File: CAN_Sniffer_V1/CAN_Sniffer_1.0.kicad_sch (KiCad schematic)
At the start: 6 parts, among them J3 Conn_01x04_Pin, J4 USB_B_Micro, U4 TPS7B8750QDDARQ1

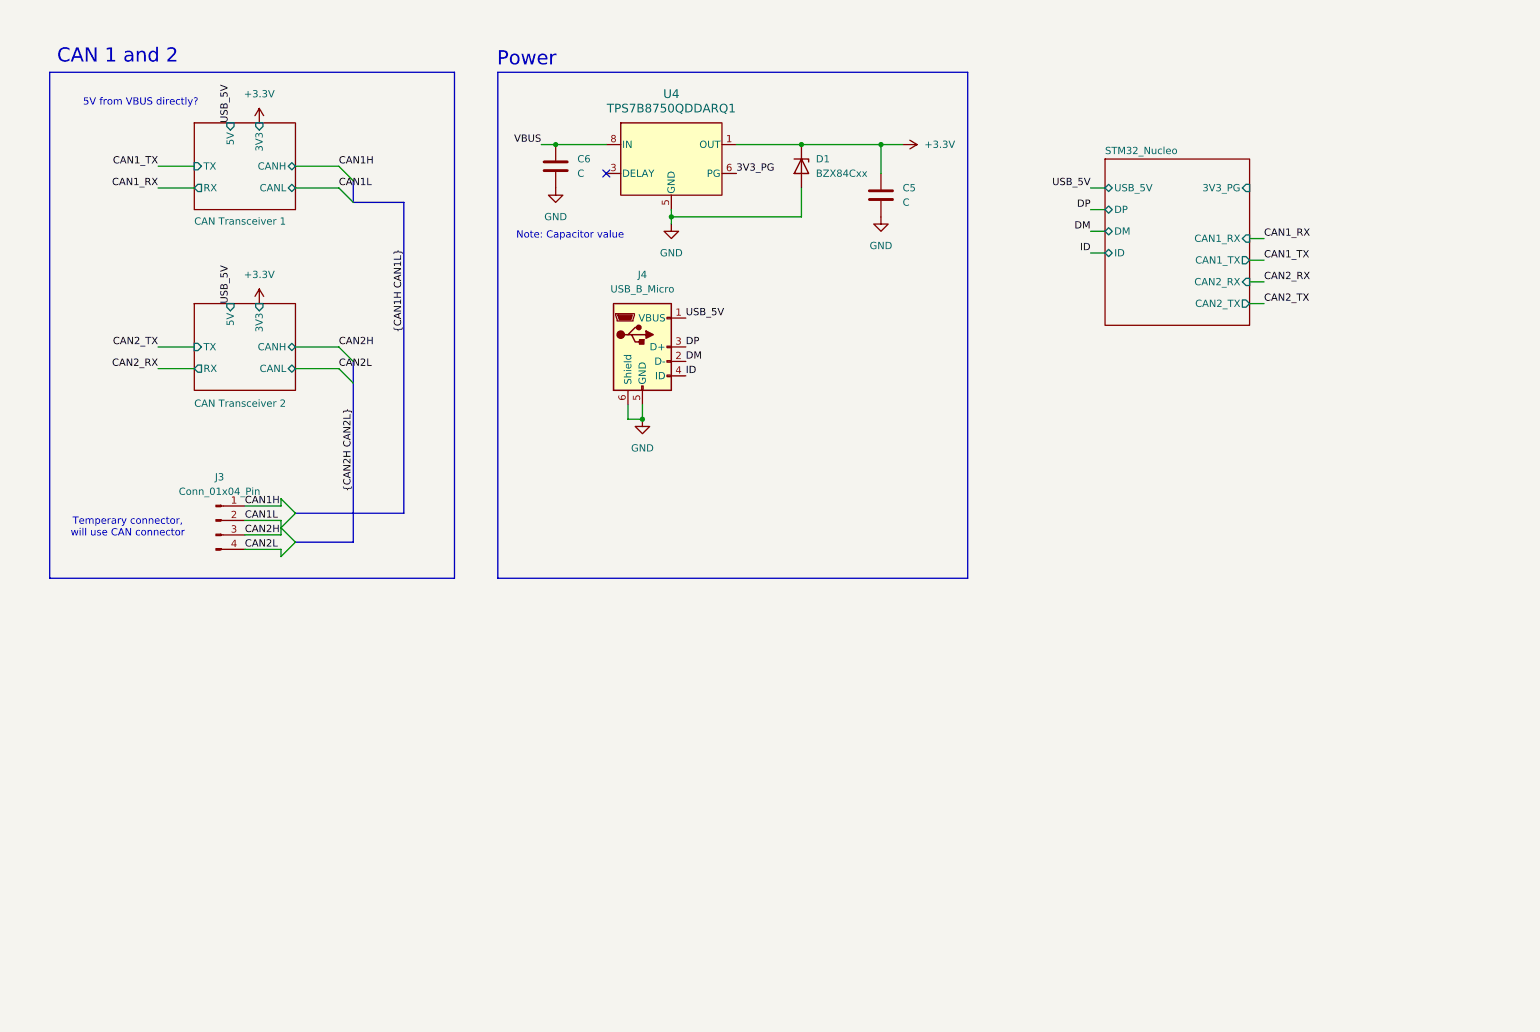
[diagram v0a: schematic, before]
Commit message: changed power schematics and STM32, added MicroSD card connector and LCD display
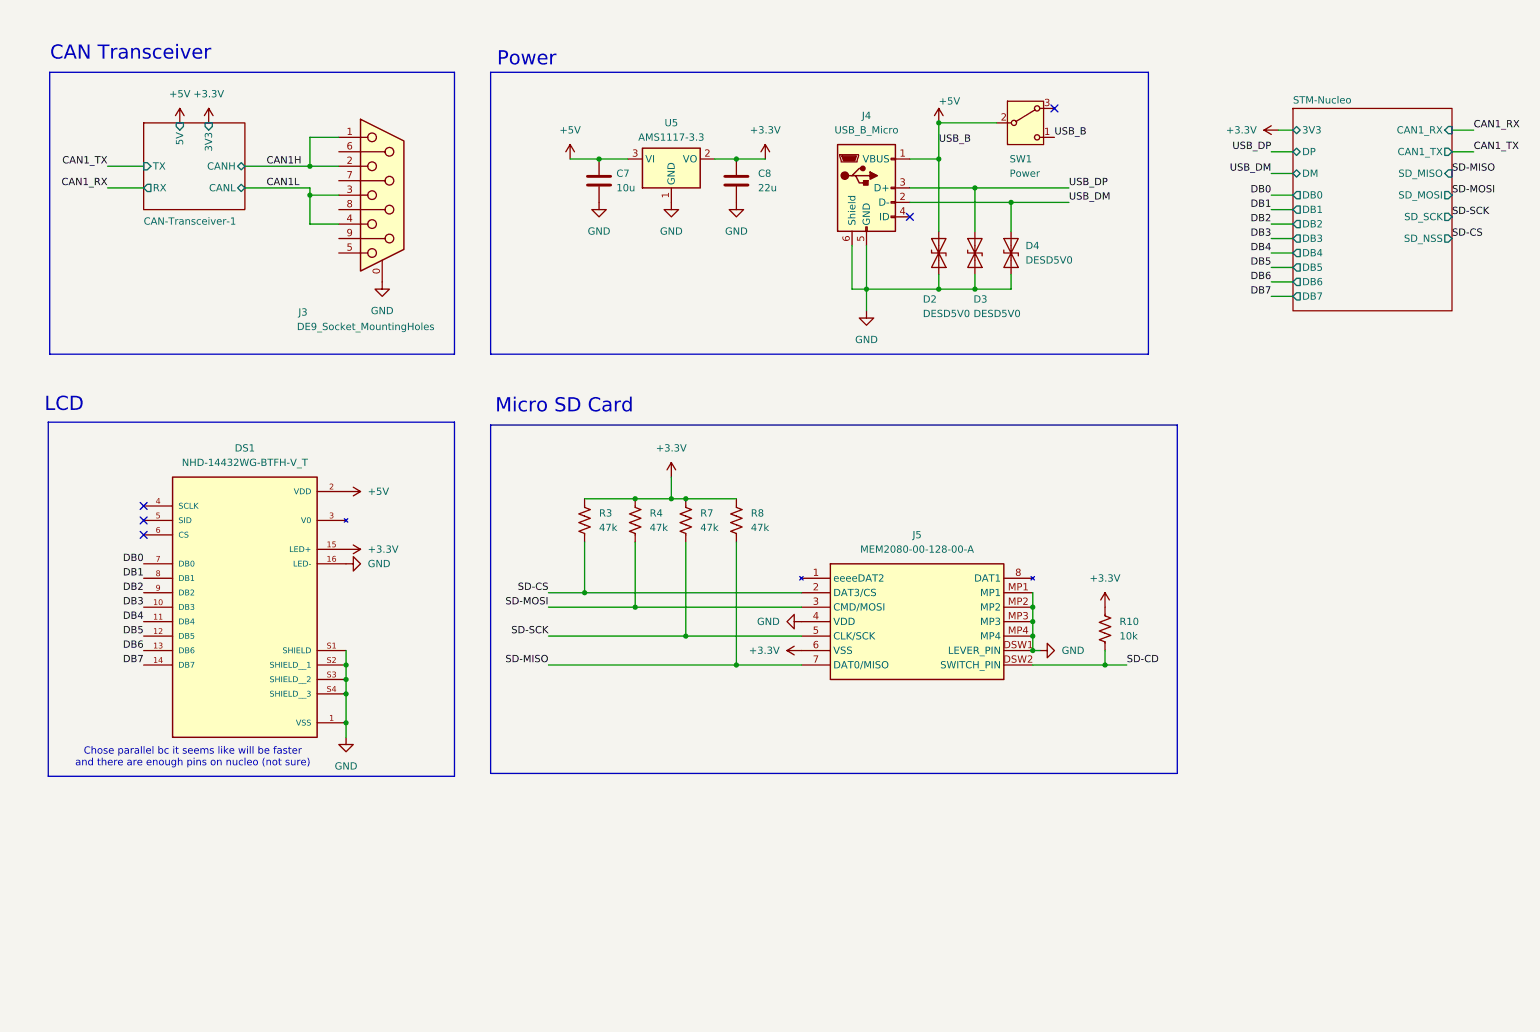
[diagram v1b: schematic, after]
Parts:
- removed C5, C6: C, symbol Device:C
- removed D1: BZX84Cxx, Package_TO_SOT_SMD:SOT-23, symbol Diode:BZX84Cxx
- removed J3: Conn_01x04_Pin, Connector_PinSocket_2.54mm:PinSocket_1x04_P2.54mm_Vertical, symbol Connector:Conn_01x04_Pin
- removed U4: TPS7B8750QDDARQ1, DDA0008J-IPC_A, symbol _LDO:TPS7B8750QDDARQ1
- added C7: 10u, Capacitor_SMD:C_0805_2012Metric_Pad1.18x1.45mm_HandSolder, symbol Device:C
- added C8: 22u, Capacitor_SMD:C_0805_2012Metric_Pad1.18x1.45mm_HandSolder, symbol Device:C
- added D2, D3, D4: DESD5V0, DESD5V0U1BA-7:IC6_AP22653AW6-7_DIO, symbol Diode:ESD131-B1-W0201
- added DS1: NHD-14432WG-BTFH-V_T, NHD-14432WG-BTFH-V_T:LCD_NHD-14432WG-BTFH-V_T, symbol NHD-14432WG-BTFH-V_T:NHD-14432WG-BTFH-V_T
- added J3: DE9_Socket_MountingHoles, Connector_Dsub:DSUB-9_Socket_Horizontal_P2.77x2.84mm_EdgePinOffset7.70mm_Housed_MountingHolesOffset9.12mm, symbol Connector:DE9_Socket_MountingHoles
- added J5: MEM2080-00-128-00-A, Mouser_Parts:MEM20800012800A, symbol Mouser_Parts:MEM2080-00-128-00-A
- added R10: 10k, Resistor_SMD:R_0805_2012Metric_Pad1.20x1.40mm_HandSolder, symbol Device:R_US
- added R3, R4, R7, R8: 47k, Resistor_SMD:R_0805_2012Metric_Pad1.20x1.40mm_HandSolder, symbol Device:R_US
- added SW1: Power, Button_Switch_SMD:Nidec_Copal_CAS-120A, symbol Switch:SW_Nidec_CAS-120A1
- added U5: AMS1117-3.3, Package_TO_SOT_SMD:SOT-223-3_TabPin2, symbol Regulator_Linear:AMS1117-3.3
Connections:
- net +3.3V: now also C8.1, DS1.15 (LED+), J5.6 (VSS), R10.2, R3.1, R4.1, R7.1, R8.1, U5.2 (VO)
- net CAN1H: now also J3.1, J3.2
- net CAN1L: now also J3.3, J3.4
- net GND: now also C7.2, C8.2, D2.1 (A1), D3.1 (A1), D4.1 (A1), DS1.1 (VSS), DS1.16 (LED-), DS1.S1 (SHIELD), DS1.S2 (SHIELD__1), DS1.S3 (SHIELD__2), DS1.S4 (SHIELD__3), J3.0 (PAD), J5.4 (VDD), J5.DSW1 (LEVER_PIN), J5.MP1, J5.MP2, J5.MP3, J5.MP4, U5.1 (GND)
- net DM renamed USB_DM
- net USB_DM: now also D4.2 (A2)
- net DP renamed USB_DP
- net USB_DP: now also D3.2 (A2)
- net ID: no longer names the net of J4.4 (ID)
- net USB_5V renamed +5V
- net +5V: now also C7.1, D2.2 (A2), DS1.2 (VDD), SW1.1 (C), SW1.2 (B), U5.3 (VI)
- new net DB0: DS1.7 (DB0)
- new net DB1: DS1.8 (DB1)
- new net DB2: DS1.9 (DB2)
- new net DB3: DS1.10 (DB3)
- new net DB4: DS1.11 (DB4)
- new net DB5: DS1.12 (DB5)
- new net DB6: DS1.13 (DB6)
- new net DB7: DS1.14 (DB7)
- new net SD-CD: J5.DSW2 (SWITCH_PIN), R10.1
- new net SD-CS: J5.2 (DAT3/CS), R3.2
- new net SD-MISO: J5.7 (DAT0/MISO), R8.2
- new net SD-MOSI: J5.3 (CMD/MOSI), R4.2
- new net SD-SCK: J5.5 (CLK/SCK), R7.2
- no-connect marks 1 -> 5
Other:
- sheet CAN Transceiver 1 renamed CAN-Transceiver-1
- removed sheet CAN Transceiver 2
- removed sheet STM32_Nucleo
- added sheet STM-Nucleo (STM32-Nucleo.kicad_sch)
- note added: "CAN Transceiver"
- note added: "Chose parallel bc it seems like will be faster and there are enough pins on nucleo (not sure)"
- note added: "LCD"
- note added: "Micro SD Card"
- note removed: "5V from VBUS directly?"
- note removed: "CAN 1 and 2"
- note removed: "Note: Capacitor value"
- note removed: "Temperary connector, will use CAN connector"
- moved on the sheet: J4

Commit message: changed power schem, pinouts, first iteration layout
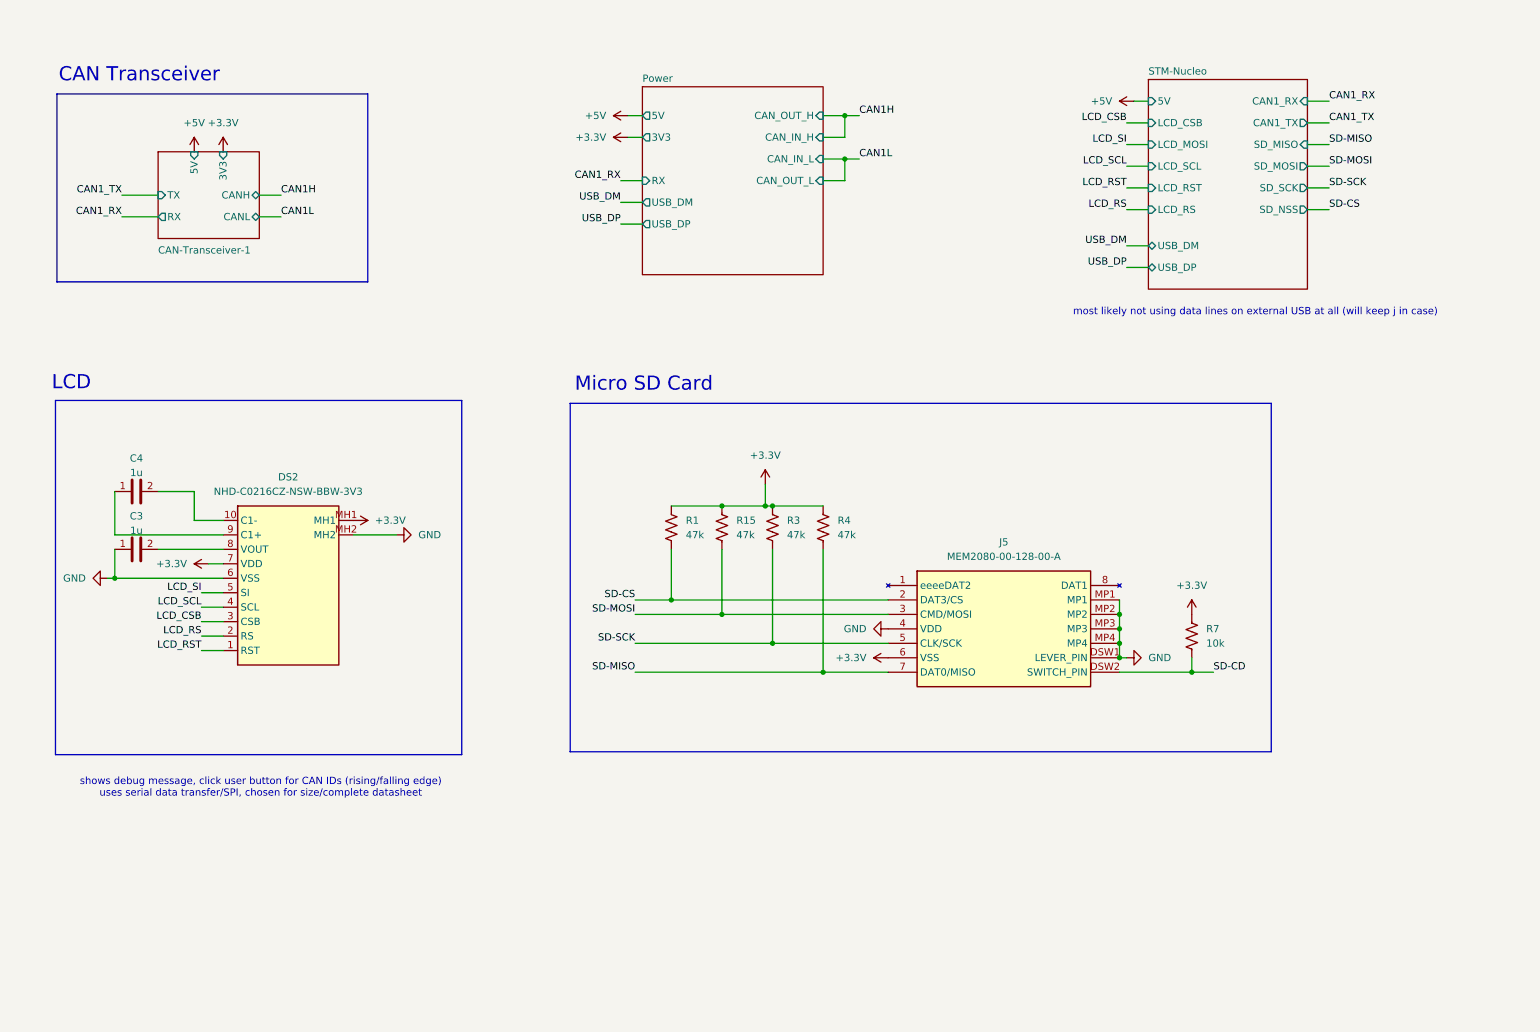
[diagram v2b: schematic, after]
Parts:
- removed C7: 10u, Capacitor_SMD:C_0805_2012Metric_Pad1.18x1.45mm_HandSolder, symbol Device:C
- removed C8: 22u, Capacitor_SMD:C_0805_2012Metric_Pad1.18x1.45mm_HandSolder, symbol Device:C
- removed D2, D3, D4: DESD5V0, DESD5V0U1BA-7:IC6_AP22653AW6-7_DIO, symbol Diode:ESD131-B1-W0201
- removed DS1: NHD-14432WG-BTFH-V_T, NHD-14432WG-BTFH-V_T:LCD_NHD-14432WG-BTFH-V_T, symbol NHD-14432WG-BTFH-V_T:NHD-14432WG-BTFH-V_T
- removed J3: DE9_Socket_MountingHoles, Connector_Dsub:DSUB-9_Socket_Horizontal_P2.77x2.84mm_EdgePinOffset7.70mm_Housed_MountingHolesOffset9.12mm, symbol Connector:DE9_Socket_MountingHoles
- removed J4: USB_B_Micro, Connector_USB:USB_Micro-AB_Molex_47590-0001, symbol Connector:USB_B_Micro
- removed R10: 10k, Resistor_SMD:R_0805_2012Metric_Pad1.20x1.40mm_HandSolder, symbol Device:R_US
- removed R3, R4, R7, R8: 47k, Resistor_SMD:R_0805_2012Metric_Pad1.20x1.40mm_HandSolder, symbol Device:R_US
- removed SW1: Power, Button_Switch_SMD:Nidec_Copal_CAS-120A, symbol Switch:SW_Nidec_CAS-120A1
- removed U5: AMS1117-3.3, Package_TO_SOT_SMD:SOT-223-3_TabPin2, symbol Regulator_Linear:AMS1117-3.3
- added C3, C4: 1u, Capacitor_SMD:C_0603_1608Metric_Pad1.08x0.95mm_HandSolder, symbol bfr_capacitors:MAJCT168BB7105KTEA01
- added DS2: NHD-C0216CZ-NSW-BBW-3V3, NHD-C0216CZ-NSW-BBW-3V3:NHDC0216CZNSWBBW3V3, symbol NHD-C0216CZ-NSW-BBW-3V3:NHD-C0216CZ-NSW-BBW-3V3
- added R1, R15, R3, R4: 47k, Resistor_SMD:R_0603_1608Metric_Pad0.98x0.95mm_HandSolder, symbol bfr_resistors:RMCF0603FT47K0
- added R7: 10k, Resistor_SMD:R_0603_1608Metric_Pad0.98x0.95mm_HandSolder, symbol bfr_resistors:RMCF0603FT10K0
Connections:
- net +3.3V: now also DS2.7 (VDD), DS2.MH1, R1.2, R15.2, R3.2, R4.2, R7.2
- net GND: now also C3.1, DS2.6 (VSS), DS2.MH2
- net SD-CD: now also R7.1
- net SD-CS: now also R1.1
- net SD-MISO: now also R4.1
- net SD-MOSI: now also R15.1
- net SD-SCK: now also R3.1
- new net: C4.2, DS2.10 (C1-)
- new net: C3.2, DS2.8 (VOUT)
- new net: C4.1, DS2.9 (C1+)
- new net LCD_CSB: DS2.3 (CSB)
- new net LCD_RS: DS2.2 (RS)
- new net LCD_RST: DS2.1 (RST)
- new net LCD_SCL: DS2.4 (SCL)
- new net LCD_SI: DS2.5 (SI)
- no-connect marks 5 -> 0
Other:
- added sheet Power (Power.kicad_sch)
- sheet STM-Nucleo ports: added 5V, LCD_CSB, LCD_MOSI, LCD_RS, LCD_RST, LCD_SCL, USB_DM, USB_DP; removed 3V3, DB0, DB1, DB2, DB3, DB4, DB5, DB6, DB7, DM, DP
- note added: "most likely not using data lines on external USB at all (will keep j in case)"
- note added: "shows debug message, click user button for CAN IDs (rising/falling edge) uses serial data transfer/SPI, chosen for size/complete datasheet"
- note removed: "Chose parallel bc it seems like will be faster and there are enough pins on nucleo (not sure)"
- note removed: "Power"
- moved on the sheet: J5

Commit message: iteration 2 routing
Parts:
- removed R7: 10k, Resistor_SMD:R_0603_1608Metric_Pad0.98x0.95mm_HandSolder, symbol bfr_resistors:RMCF0603FT10K0
- added C14: 10u, Capacitor_SMD:C_0603_1608Metric_Pad1.08x0.95mm_HandSolder, symbol bfr_capacitors:CL10A106MA8NRNC
- added C7, C8, C9: 100n, Capacitor_SMD:C_0603_1608Metric_Pad1.08x0.95mm_HandSolder, symbol bfr_capacitors:06035C104KAT2A
- added R12: 10k, Resistor_SMD:R_0603_1608Metric_Pad0.98x0.95mm_HandSolder, symbol bfr_resistors:RMCF0603FT10K0
- added TP12: LCD-SI, TestPoint:TestPoint_Pad_D1.0mm, symbol Connector:TestPoint
- added TP13, TP14: LCD-SCL, TestPoint:TestPoint_Pad_D1.0mm, symbol Connector:TestPoint
- added TP15: LCD-RST, TestPoint:TestPoint_Pad_D1.0mm, symbol Connector:TestPoint
- added TP16, TP22: LCD_3V3, TestPoint:TestPoint_Pad_D1.0mm, symbol Connector:TestPoint
- added TP17: LCD_VOUT, TestPoint:TestPoint_Pad_D1.0mm, symbol Connector:TestPoint
- added TP8: LCD-RS, TestPoint:TestPoint_Pad_D1.0mm, symbol Connector:TestPoint
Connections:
- net +3.3V: now also J5.4 (VDD), C14.1, C7.1, C8.1, C9.1, R12.2, TP16.1; no longer J5.6 (VSS)
- net GND: now also J5.6 (VSS), C14.2, C7.2, C8.2, C9.2; no longer J5.4 (VDD)
- net LCD_CSB: now also TP14.1
- net LCD_RS: now also TP8.1
- net LCD_RST: now also TP15.1
- net LCD_SCL: now also TP13.1
- net LCD_SI: now also TP12.1
- net LCD_VOUT: now reaches C3.2, DS2.8 (VOUT)
- net LCD_VOUT: now also TP17.1
- net LCD_C1: now reaches C4.1, DS2.9 (C1+)
- net LCD_C1: now also TP22.1
- net SD-CD renamed SD_CD
- net SD_CD: now also R12.1
- net SD-CS renamed SD_CS
- net SD-MISO renamed SD_MISO
- net SD-MOSI renamed SD_MOSI
- net SD-SCK renamed SD_SCK
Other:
- sheet CAN-Transceiver-1 renamed CAN-Transceiver
- sheet Power ports: added CANH, CANL, CAN_RX, U5V; removed 3V3, CAN_IN_H, CAN_IN_L, CAN_OUT_H, CAN_OUT_L, RX, USB_DM, USB_DP
- sheet STM-Nucleo ports: added 3V3, CAN_RX, CAN_TX, SD_CD, U5V; removed CAN1_RX, CAN1_TX, USB_DM, USB_DP
- note added: "Power"
- note removed: "most likely not using data lines on external USB at all (will keep j in case)"
- note removed: "shows debug message, click user button for CAN IDs (rising/falling edge) uses serial data transfer/SPI, chosen for size/complete datasheet"
- moved on the sheet: C3, C4, DS2, J5, R1, R15, R3, R4

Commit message: sync changes
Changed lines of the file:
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@@
-	)
-	(bus_entry
-		(at 130.81 64.77)
-		(size -2.54 -2.54)
-		(stroke
-			(width 0)
-			(type default)
-		)
 	)
 	(bus_entry
@@
 	(bus
 		(pts
-			(xy 130.81 64.77) (xy 130.81 73.66)
+			(xy 130.81 62.23) (xy 130.81 73.66)
 		)
 		(stroke
@@
 		)
 	)
-	(wire
-		(pts
-			(xy 160.02 128.27) (xy 161.29 128.27)
-		)
-		(stroke
-			(width 0)
-			(type default)
-		)
-	)
 	(bus
 		(pts
@@
 		)
 	)
-	(bus
-		(pts
-			(xy 130.81 62.23) (xy 130.81 64.77)
+	(wire
+		(pts
+			(xy 161.29 129.54) (xy 161.29 128.27)
 		)
 		(stroke
@@
 		(pts
 			(xy 165.1 36.83) (xy 173.99 36.83)
-		)
-		(stroke
-			(width 0)
-			(type default)
-		)
-	)
-	(wire
-		(pts
-			(xy 123.19 62.23) (xy 128.27 62.23)
 		)
 		(stroke
@@
 	(label "SD_MOSI"
 		(at 128.27 48.26 0)
-		(effects
-			(font
-				(size 1.27 1.27)
-			)
-			(justify left bottom)
-		)
-	)
-	(label "SD_CD"
-		(at 123.19 62.23 0)
 		(effects
 			(font
@@
 	(symbol
 		(lib_id "power:GND")
-		(at 160.02 128.27 270)
+		(at 161.29 129.54 0)
 		(unit 1)
 		(exclude_from_sim no)
@@
 		(dnp no)
 		(property "Reference" "#PWR018"
-			(at 153.67 128.27 0)
+			(at 161.29 135.89 0)
 			(effects
 				(font
@@
 		)
 		(property "Value" "GND"
-			(at 156.21 128.2699 90)
+			(at 161.2899 133.35 0)
 			(effects
 				(font
@@
 		)
 		(property "Footprint" ""
-			(at 160.02 128.27 0)
+			(at 161.29 129.54 0)
 			(effects
 				(font
@@
 		)
 		(property "Datasheet" ""
-			(at 160.02 128.27 0)
+			(at 161.29 129.54 0)
 			(effects
 				(font
@@
 		)
 		(property "Description" "Power symbol creates a global label with name \"GND\" , ground"
-			(at 160.02 128.27 0)
-			(effects
-				(font
+			(at 161.29 129.54 0)
+			(effects
+				(font
